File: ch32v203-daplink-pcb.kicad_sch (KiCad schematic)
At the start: 25 parts, among them J1 USB2.0_C_v3, J2 DAPLink-SWD-Send-10Pin, J3 DAPLink-SWD-Send-6Pin, U1 STM32V103C8T6, U2 AMS1117-3.3, Y2 8M

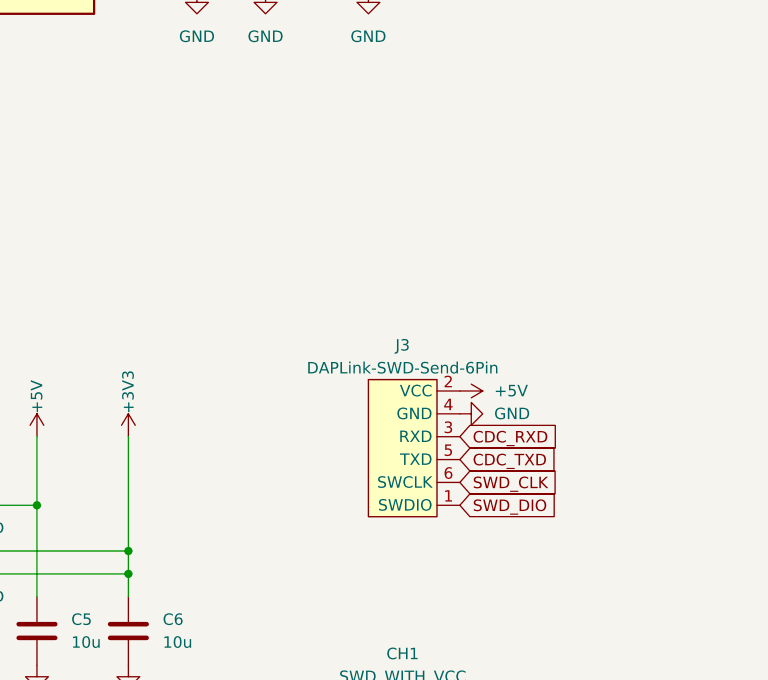
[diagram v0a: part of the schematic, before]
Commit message: for Arduino UNO R4
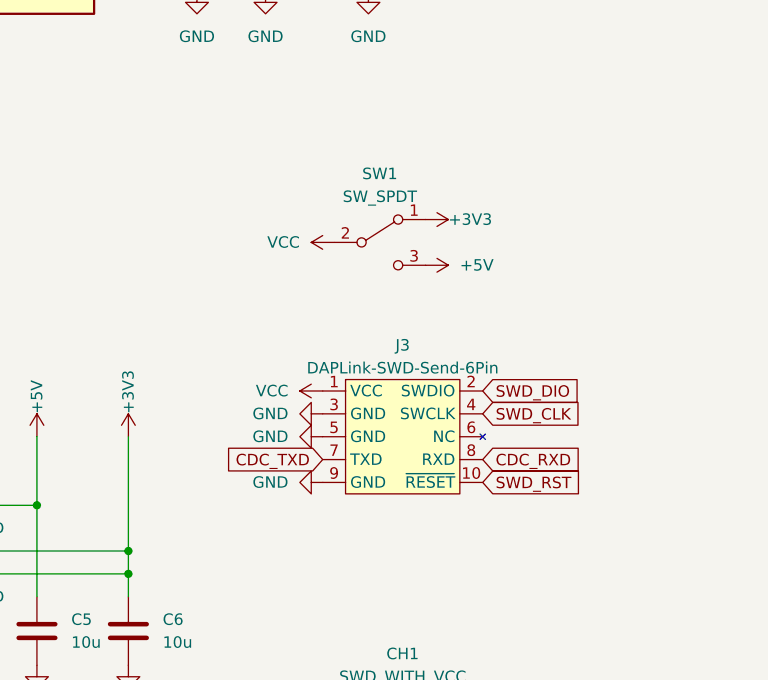
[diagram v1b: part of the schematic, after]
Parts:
- added SW1: SW_SPDT, $74th:Slide_Switch, symbol Switch:SW_SPDT
- J3: footprint $74th:BoxPinHeader_2x03_P1.27mm_Vertical -> $74th:BoxPinHeader_2x05_P1.27mm_Vertical; symbol $74th:DAPLink-SWD-Send-6Pin -> $74th:SWD-Debugger_Side-10Pin
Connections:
- net +3V3: now also SW1.1 (A)
- net +5V: now also SW1.3 (C); no longer J3.2 (VCC)
- net CDC_RXD: now also J3.8 (RXD); no longer J3.3 (RXD)
- net CDC_TXD: now also J3.7 (TXD); no longer J3.5 (TXD)
- net GND: now also J3.3 (GND), J3.5 (GND), J3.9 (GND); no longer J3.4 (GND)
- net SWD_CLK: now also J3.4 (SWCLK); no longer J3.6 (SWCLK)
- net SWD_DIO: now also J3.2 (SWDIO); no longer J3.1 (SWDIO)
- net SWD_RST: now also J3.10 (~{RESET})
- new net VCC: J3.1 (VCC), SW1.2 (B)

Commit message: v1.1.0
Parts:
- J3: renamed from J2; footprint $74th:DAPLink-SWD -> $74th:Side-2x5P-PinHeader-Right; symbol $74th:DAPLink-SWD-Send-10Pin -> $74th:DAPLink-SWD-Send-Side10Pin
- renumbered C8 to C1, C7 to C2, C6 to C3, C5 to C4, C10 to C5, C3 to C6, C9 to C7, C2 to C8, C4 to C9, D2 to D1, D1 to D2, J3 to J2, R4 to R1, R3 to R2, R1 to R3, R8 to R4, R2 to R5, R7 to R6, R6 to R7, Y2 to Y1
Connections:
- net +3V3: now also J3.6 (TXD); no longer J3.7 (3V3)
- net +5V: now also J3.2 (5V); no longer J3.10 (5V)
- net CDC_TXD: now also J3.3 (SWD); no longer J3.2 (TXD)
- net GND: now also J3.10 (3V3), J3.4 (RXD); no longer J3.6 (GND), J3.9 (GND)
- net SWD_CLK: now also J3.7 (GND); no longer J3.4 (SCK)
- net SWD_DIO: now also J3.5 (SCK); no longer J3.3 (SWD)
- net SWD_RST: now also J3.9 (RST); no longer J3.5 (RST)

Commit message: fix
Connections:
- net +3V3: now also R2.1; no longer R3.1
- net BOOT0: now also R3.1; no longer R3.2
- net GND: now also R3.2; no longer R2.2
- net RST: now also R2.2; no longer R2.1
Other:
- moved on the sheet: R2
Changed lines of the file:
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@@
     (stroke (width 0) (type default))
   )
-  (wire (pts (xy 90.17 33.02) (xy 93.98 33.02))
+  (wire (pts (xy 90.17 25.4) (xy 93.98 25.4))
     (stroke (width 0) (type default))
   )
@@
     )
   )
-  (global_label "BOOT0" (shape input) (at 93.98 33.02 0) (fields_autoplaced)
+  (global_label "BOOT0" (shape input) (at 93.98 25.4 0) (fields_autoplaced)
     (effects (font (size 1.27 1.27)) (justify left))
-    (property "Intersheetrefs" "${INTERSHEET_REFS}" (at 102.9939 33.02 0)
-      (effects (font (size 1.27 1.27)) (justify left) hide)
-    )
-    (property "シート間のリファレンス" "${INTERSHEET_REFS}" (at 93.98 35.2108 0)
+    (property "Intersheetrefs" "${INTERSHEET_REFS}" (at 102.9939 25.4 0)
+      (effects (font (size 1.27 1.27)) (justify left) hide)
+    )
+    (property "シート間のリファレンス" "${INTERSHEET_REFS}" (at 93.98 27.5908 0)
       (effects (font (size 1.27 1.27)) (justify left) hide)
     )
@@
     )
   )
+  (symbol (lib_id "power:+3V3") (at 31.75 111.76 0) (unit 1)
+    (in_bom yes) (on_board yes) (dnp no) (fields_autoplaced)
+    (property "Reference" "#PWR06" (at 31.75 115.57 0)
+      (effects (font (size 1.27 1.27)) hide)
+    )
+    (property "Value" "+3V3" (at 31.75 106.68 0)
+      (effects (font (size 1.27 1.27)))
+    )
+    (property "Footprint" "" (at 31.75 111.76 0)
+      (effects (font (size 1.27 1.27)) hide)
+    )
+    (property "Datasheet" "" (at 31.75 111.76 0)
+      (effects (font (size 1.27 1.27)) hide)
+    )
+    (pin "1")
+    (instances
+      (project "ch32v203-daplink-pcb"
+        (path "/159a7907-fbf4-4cbf-a918-6615e794ddfa"
+          (reference "#PWR06") (unit 1)
+        )
+      )
+      (project "ch32v203-promicro"
+        (path "/afcc1797-22e9-4a4e-a23b-4101109b7b33"
+          (reference "#PWR0117") (unit 1)
+        )
+      )
+    )
+  )
   (symbol (lib_id "Device:R") (at 90.17 29.21 0) (unit 1)
     (in_bom yes) (on_board yes) (dnp no) (fields_autoplaced)
@@
     )
   )
-  (symbol (lib_id "Device:R") (at 31.75 123.19 0) (unit 1)
-    (in_bom yes) (on_board yes) (dnp no) (fields_autoplaced)
-    (property "Reference" "R2" (at 34.29 121.9199 0)
-      (effects (font (size 1.27 1.27)) (justify left))
-    )
-    (property "Value" "10k" (at 34.29 124.4599 0)
-      (effects (font (size 1.27 1.27)) (justify left))
-    )
-    (property "Footprint" "$74th:Register_0603_1608" (at 29.972 123.19 90)
-      (effects (font (size 1.27 1.27)) hide)
-    )
-    (property "Datasheet" "~" (at 31.75 123.19 0)
+  (symbol (lib_id "Device:R") (at 31.75 115.57 0) (unit 1)
+    (in_bom yes) (on_board yes) (dnp no) (fields_autoplaced)
+    (property "Reference" "R2" (at 34.29 114.2999 0)
+      (effects (font (size 1.27 1.27)) (justify left))
+    )
+    (property "Value" "10k" (at 34.29 116.8399 0)
+      (effects (font (size 1.27 1.27)) (justify left))
+    )
+    (property "Footprint" "$74th:Register_0603_1608" (at 29.972 115.57 90)
+      (effects (font (size 1.27 1.27)) hide)
+    )
+    (property "Datasheet" "~" (at 31.75 115.57 0)
       (effects (font (size 1.27 1.27)) hide)
     )
@@
         (path "/afcc1797-22e9-4a4e-a23b-4101109b7b33"
           (reference "R6") (unit 1)
-        )
-      )
-    )
-  )
-  (symbol (lib_id "power:GND") (at 31.75 127 0) (unit 1)
-    (in_bom yes) (on_board yes) (dnp no) (fields_autoplaced)
-    (property "Reference" "#PWR06" (at 31.75 133.35 0)
-      (effects (font (size 1.27 1.27)) hide)
-    )
-    (property "Value" "GND" (at 34.29 128.2699 0)
-      (effects (font (size 1.27 1.27)) (justify left))
-    )
-    (property "Footprint" "" (at 31.75 127 0)
-      (effects (font (size 1.27 1.27)) hide)
-    )
-    (property "Datasheet" "" (at 31.75 127 0)
-      (effects (font (size 1.27 1.27)) hide)
-    )
-    (pin "1")
-    (instances
-      (project "ch32v203-daplink-pcb"
-        (path "/159a7907-fbf4-4cbf-a918-6615e794ddfa"
-          (reference "#PWR06") (unit 1)
-        )
-      )
-      (project "ch32v203-promicro"
-        (path "/afcc1797-22e9-4a4e-a23b-4101109b7b33"
-          (reference "#PWR01") (unit 1)
         )
       )
@@
         (path "/afcc1797-22e9-4a4e-a23b-4101109b7b33"
           (reference "D1") (unit 1)
-        )
-      )
-    )
-  )
-  (symbol (lib_id "power:+3V3") (at 90.17 25.4 0) (unit 1)
-    (in_bom yes) (on_board yes) (dnp no) (fields_autoplaced)
-    (property "Reference" "#PWR03" (at 90.17 29.21 0)
-      (effects (font (size 1.27 1.27)) hide)
-    )
-    (property "Value" "+3V3" (at 90.17 20.32 0)
-      (effects (font (size 1.27 1.27)))
-    )
-    (property "Footprint" "" (at 90.17 25.4 0)
-      (effects (font (size 1.27 1.27)) hide)
-    )
-    (property "Datasheet" "" (at 90.17 25.4 0)
-      (effects (font (size 1.27 1.27)) hide)
-    )
-    (pin "1")
-    (instances
-      (project "ch32v203-daplink-pcb"
-        (path "/159a7907-fbf4-4cbf-a918-6615e794ddfa"
-          (reference "#PWR03") (unit 1)
-        )
-      )
-      (project "ch32v203-promicro"
-        (path "/afcc1797-22e9-4a4e-a23b-4101109b7b33"
-          (reference "#PWR0128") (unit 1)
         )
       )
@@
         )
       )
+    )
+  )
+  (symbol (lib_id "power:GND") (at 90.17 33.02 0) (unit 1)
+    (in_bom yes) (on_board yes) (dnp no) (fields_autoplaced)
+    (property "Reference" "#PWR03" (at 90.17 39.37 0)
+      (effects (font (size 1.27 1.27)) hide)
+    )
+    (property "Value" "GND" (at 92.71 34.2899 0)
+      (effects (font (size 1.27 1.27)) (justify left))
+    )
+    (property "Footprint" "" (at 90.17 33.02 0)
+      (effects (font (size 1.27 1.27)) hide)
+    )
+    (property "Datasheet" "" (at 90.17 33.02 0)
+      (effects (font (size 1.27 1.27)) hide)
+    )
+    (pin "1")
+    (instances
+      (project "ch32v203-daplink-pcb"
+        (path "/159a7907-fbf4-4cbf-a918-6615e794ddfa"
+          (reference "#PWR03") (unit 1)
+        )
+      )
+      (project "ch32v203-promicro"
+        (path "/afcc1797-22e9-4a4e-a23b-4101109b7b33"
+          (reference "#PWR02") (unit 1)
+        )
+      )

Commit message: fix semantics
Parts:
- R2, R3: value 10k -> 10k(NC)
- U1: value STM32V103C8T6 -> CH32V203C8T6
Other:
- note added: "DAPLink Pin"
- note added: "Debugger MCU SWD"
- note added: "MCU"
- note added: "SWD 10Pin"
- note added: "USB"
- note added: "VCC Select"
- title: (none) -> CH32V203 DapLink
- moved on the sheet: C1, C3, C4, C5, C6, C7, C8, C9, CH1, D1, D2, J1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
